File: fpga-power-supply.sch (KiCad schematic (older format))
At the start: 93 parts, among them U14 XC7A100T-FGG484

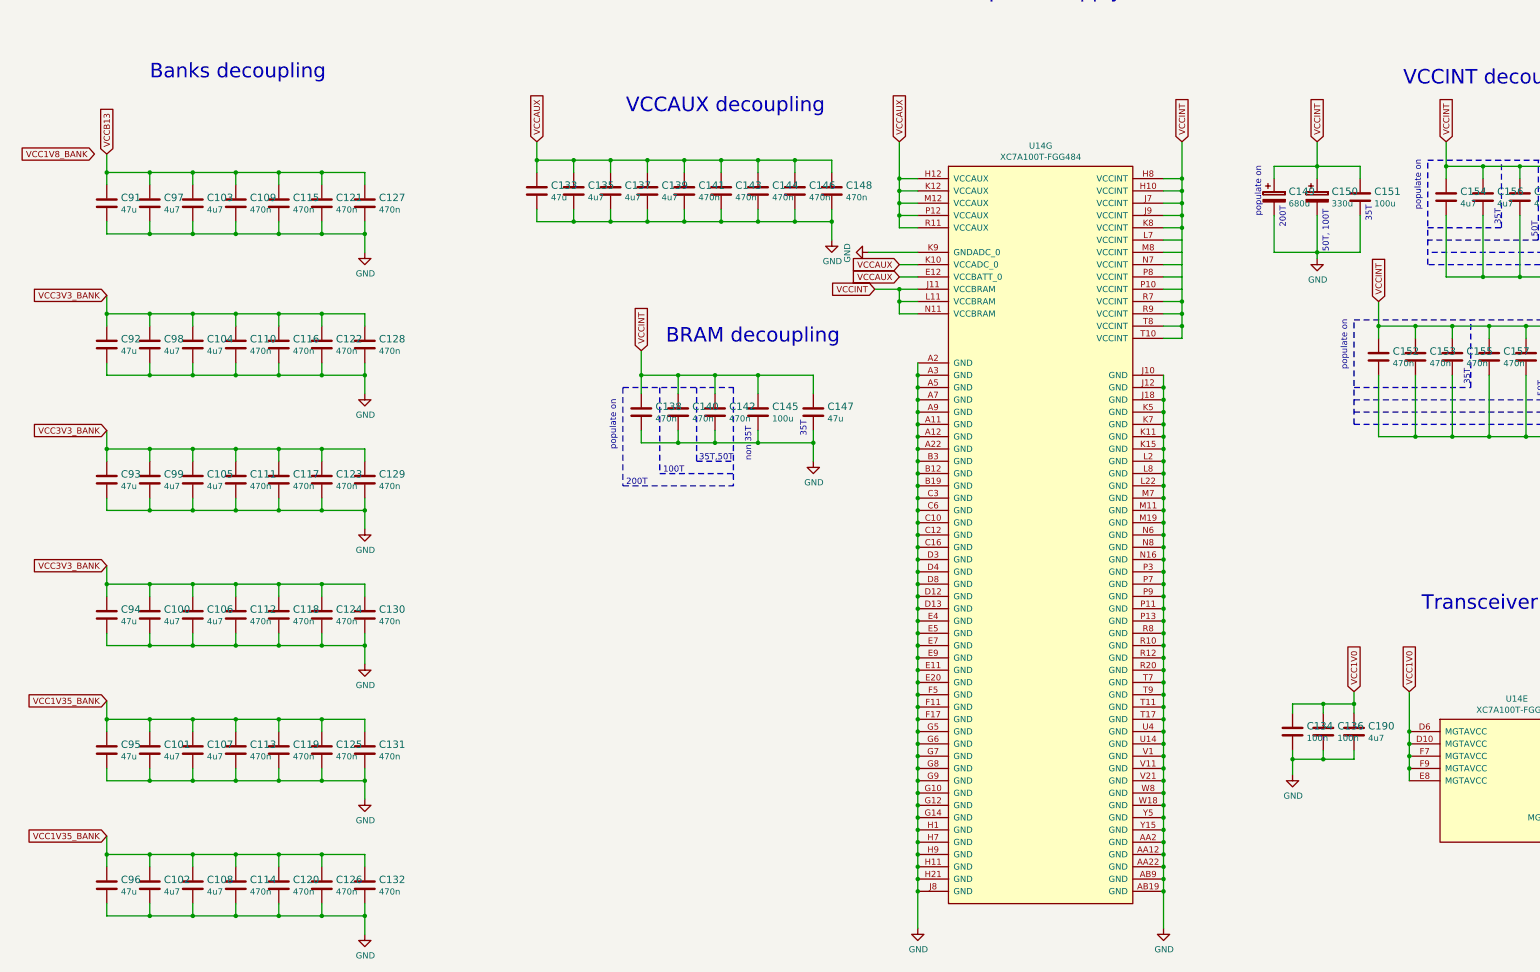
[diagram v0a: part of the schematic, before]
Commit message: Updated voltage supply labels, connected gpios left
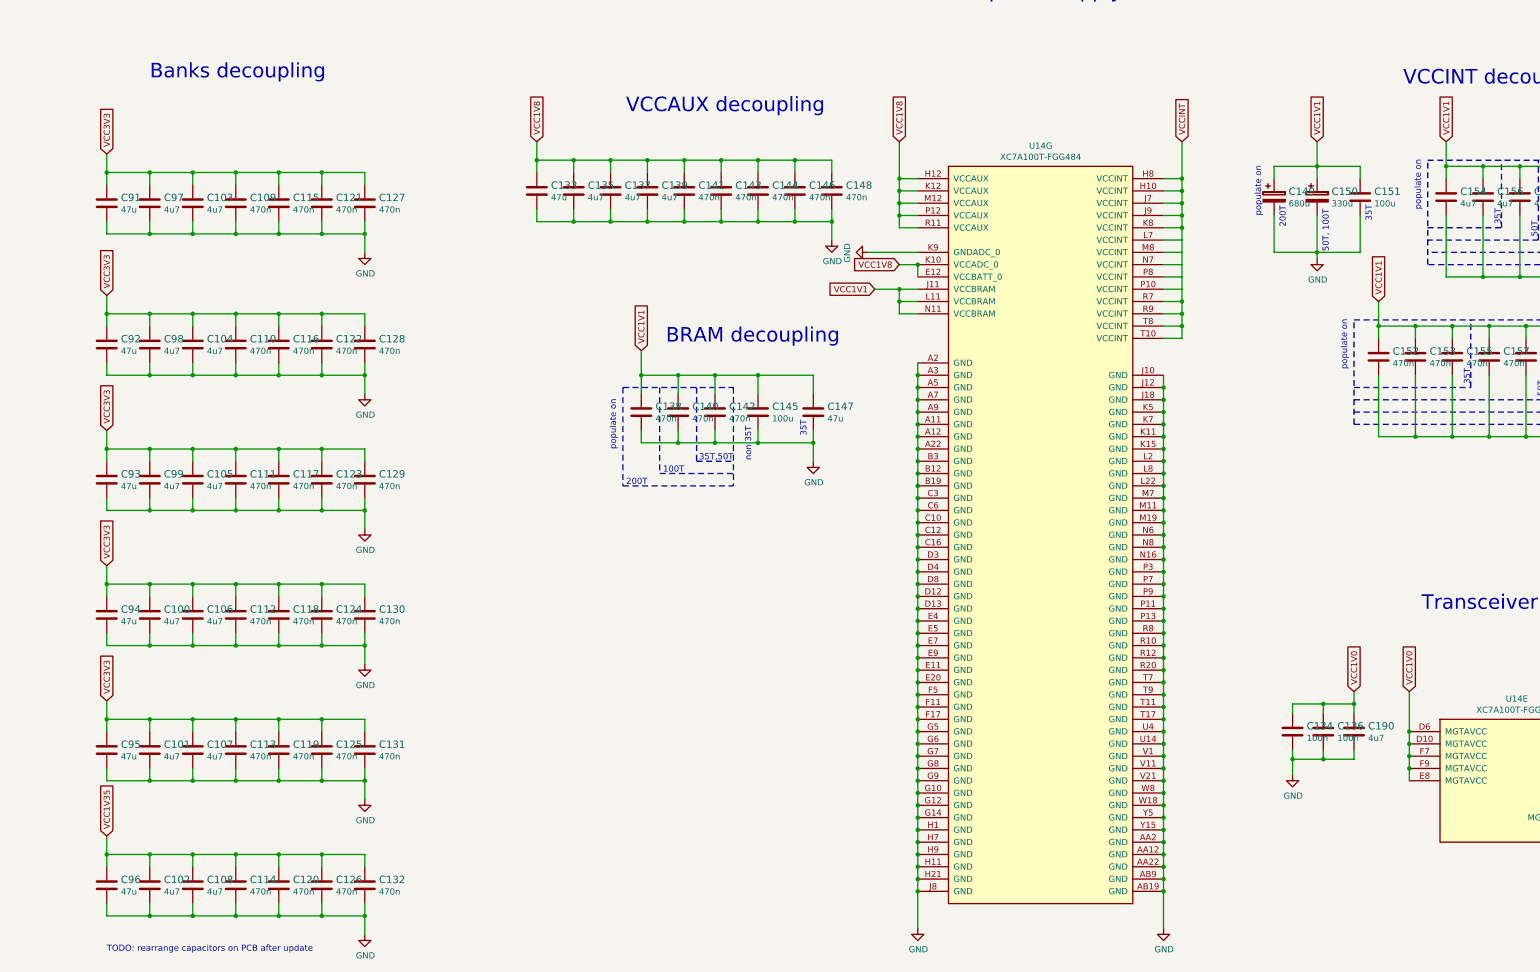
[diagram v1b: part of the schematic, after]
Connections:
- net VCCB13 is gone; now on net VCC3V3: C103.1, C109.1, C115.1, C121.1, C127.1, C91.1, C97.1
- net VCCINT: no longer C138.1, C140.1, C142.1, C145.1, C147.1, C149.1, C150.1, C151.1, C152.1, C153.1, C154.1, C155.1, C156.1, C157.1, C158.1, C159.1, C160.1, C161.1, C162.1, C163.1, C164.1, C165.1, C166.1, C167.1, C168.1, C169.1, C170.1, C171.1, C172.1, C173.1, C174.1, C175.1, C176.1, C177.1, U14.J11 (VCCBRAM), U14.L11 (VCCBRAM), U14.N11 (VCCBRAM)
- net VCC1V35_BANK renamed VCC1V35
- net VCC1V35: no longer C101.1, C107.1, C113.1, C119.1, C125.1, C131.1, C95.1
- net VCC3V3_BANK renamed VCC3V3
- net VCC3V3: now also C101.1, C107.1, C113.1, C119.1, C125.1, C131.1, C95.1
- net VCCAUX renamed VCC1V8
- new net VCC1V1: C138.1, C140.1, C142.1, C145.1, C147.1, C149.1, C150.1, C151.1, C152.1, C153.1, C154.1, C155.1, C156.1, C157.1, C158.1, C159.1, C160.1, C161.1, C162.1, C163.1, C164.1, C165.1, C166.1, C167.1, C168.1, C169.1, C170.1, C171.1, C172.1, C173.1, C174.1, C175.1, C176.1, C177.1, U14.J11 (VCCBRAM), U14.L11 (VCCBRAM), U14.N11 (VCCBRAM)
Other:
- note added: "TODO: rearrange capacitors on PCB after update"
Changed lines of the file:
@@
 	1150 2850 1150 2700
 Connection ~ 1150 2850
-Text GLabel 1150 2700 1    50   Input ~ 0
-VCCB13
 $Comp
 L artix-dc-scm:C_47u_1210 C?
@@
 	9900 4100 9900 4200
 Wire Wire Line
-	7750 3700 7600 3700
-Wire Wire Line
 	7750 3600 7600 3600
 $Comp
@@
 Text Notes 5375 2375 0    118  ~ 0
 VCCAUX decoupling
-Text GLabel 4650 2600 1    50   Input ~ 0
-VCCAUX
-Text GLabel 7600 2600 1    50   Input ~ 0
-VCCAUX
-Text GLabel 7600 3600 0    50   Input ~ 0
-VCCAUX
-Text GLabel 7600 3700 0    50   Input ~ 0
-VCCAUX
 Text GLabel 7400 3800 0    50   Input ~ 0
-VCCINT
-Text GLabel 5500 4300 1    50   Input ~ 0
-VCCINT
+VCC1V1
 Text GLabel 9900 2600 1    50   Input ~ 0
 VCCINT
-Text GLabel 11000 2600 1    50   Input ~ 0
-VCCINT
-Text GLabel 12050 2600 1    50   Input ~ 0
-VCCINT
-Text GLabel 11500 3900 1    50   Input ~ 0
-VCCINT
-Text GLabel 1050 2700 0    50   Input ~ 0
-VCC1V8_BANK
-Text GLabel 1150 4950 0    50   Input ~ 0
-VCC3V3_BANK
-Text GLabel 1150 6050 0    50   Input ~ 0
-VCC3V3_BANK
-Text GLabel 1150 7150 0    50   Input ~ 0
-VCC1V35_BANK
-Text GLabel 1150 8250 0    50   Input ~ 0
-VCC1V35_BANK
+Text GLabel 1150 7150 1    50   Input ~ 0
+VCC3V3
+Text GLabel 1150 8250 1    50   Input ~ 0
+VCC1V35
 $Comp
 L artix-dc-scm:C_4u7_0603 C?
@@
 Wire Wire Line
 	7350 3500 7750 3500
-Text GLabel 1150 3850 0    50   Input ~ 0
-VCC3V3_BANK
+Text GLabel 1150 3850 1    50   Input ~ 0
+VCC3V3
 $Comp
 L artix-dc-scm:XC7A100T-FGG484 U?
@@
 Text Notes 11850 6425 0    118  ~ 0
 Transceiver supply
+Text GLabel 7600 2600 1    50   Input ~ 0
+VCC1V8
+Text GLabel 7600 3600 0    50   Input ~ 0
+VCC1V8
+Wire Wire Line
+	7750 3600 7750 3700
+Connection ~ 7750 3600
+Text GLabel 4650 2600 1    50   Input ~ 0
+VCC1V8
+Text GLabel 1150 2700 1    50   Input ~ 0
+VCC3V3
+Text GLabel 1150 4950 1    50   Input ~ 0
+VCC3V3
+Text GLabel 1150 6050 1    50   Input ~ 0
+VCC3V3
+Text GLabel 5500 4300 1    50   Input ~ 0
+VCC1V1
+Text GLabel 11000 2600 1    50   Input ~ 0
+VCC1V1
+Text GLabel 12050 2600 1    50   Input ~ 0
+VCC1V1
+Text GLabel 11500 3900 1    50   Input ~ 0
+VCC1V1
+Text Notes 1150 9200 0    50   ~ 0
+TODO: rearrange capacitors on PCB after update
 $EndSCHEMATC

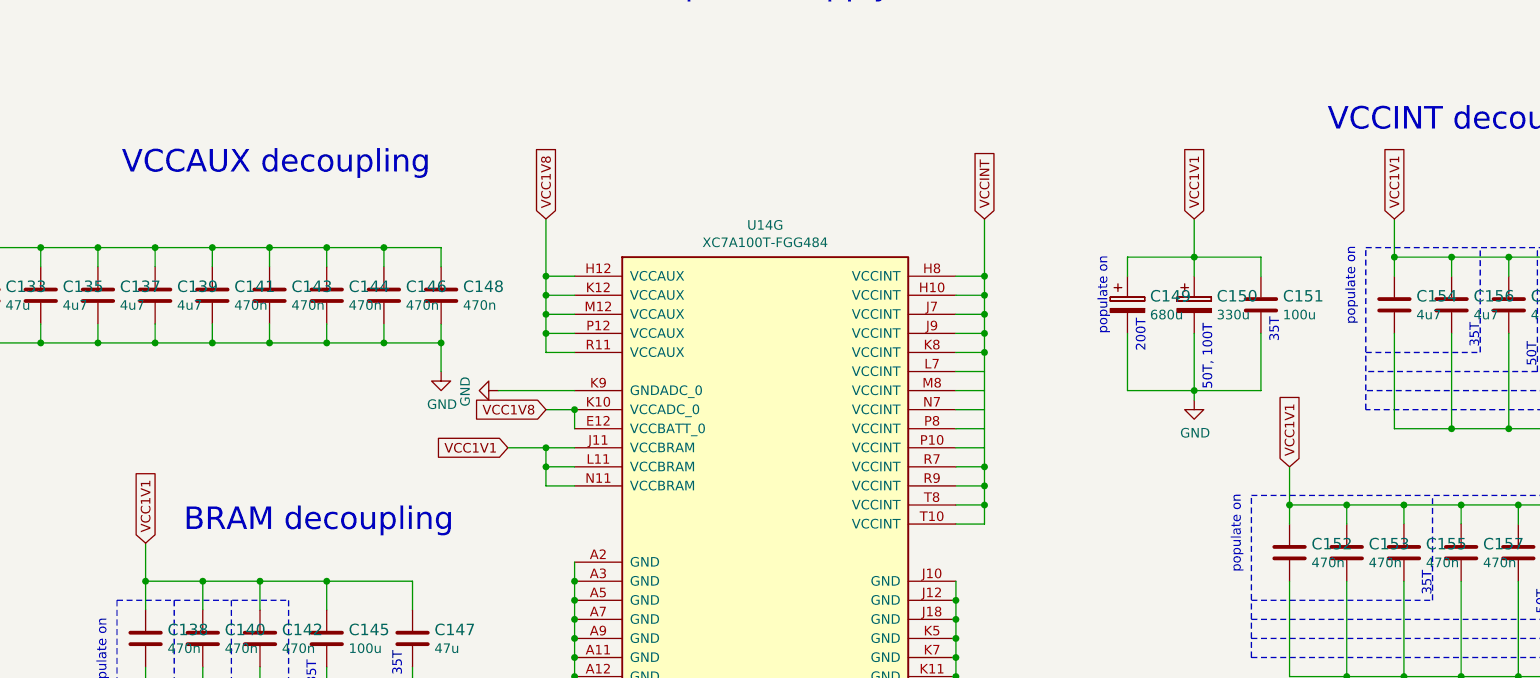
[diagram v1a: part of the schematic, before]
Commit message: Added power planes, set M.2 mounting hole position
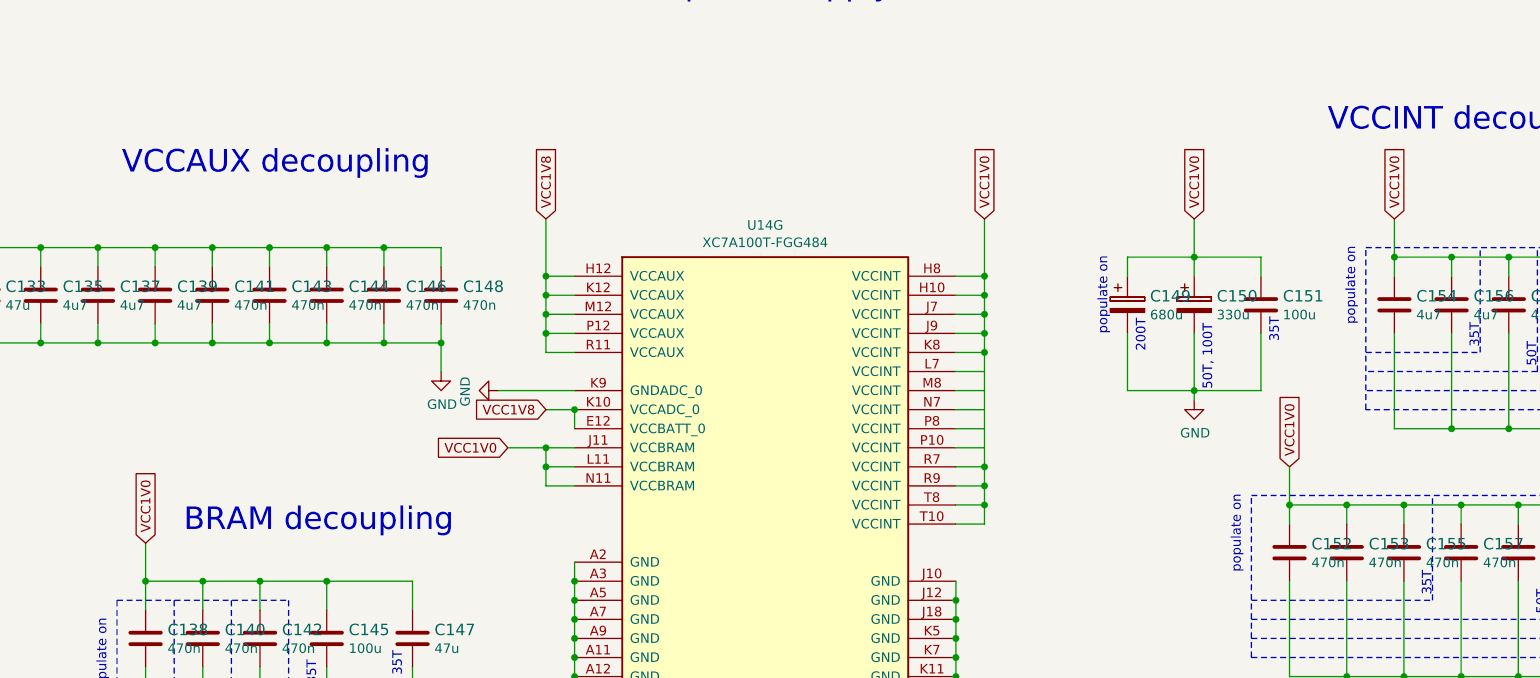
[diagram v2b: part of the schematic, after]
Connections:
- net VCC1V1 is gone; now on net VCC1V0: C138.1, C140.1, C142.1, C145.1, C147.1, C149.1, C150.1, C151.1, C152.1, C153.1, C154.1, C155.1, C156.1, C157.1, C158.1, C159.1, C160.1, C161.1, C162.1, C163.1, C164.1, C165.1, C166.1, C167.1, C168.1, C169.1, C170.1, C171.1, C172.1, C173.1, C174.1, C175.1, C176.1, C177.1, U14.J11 (VCCBRAM), U14.L11 (VCCBRAM), U14.N11 (VCCBRAM)
- net VCCINT is gone; now on net VCC1V0: U14.H10 (VCCINT), U14.H8 (VCCINT), U14.J7 (VCCINT), U14.J9 (VCCINT), U14.K8 (VCCINT), U14.R7 (VCCINT), U14.R9 (VCCINT), U14.T10 (VCCINT), U14.T8 (VCCINT)
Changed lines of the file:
@@
 VCCAUX decoupling
 Text GLabel 7400 3800 0    50   Input ~ 0
-VCC1V1
-Text GLabel 9900 2600 1    50   Input ~ 0
-VCCINT
+VCC1V0
 Text GLabel 1150 7150 1    50   Input ~ 0
 VCC3V3
@@
 VCC3V3
 Text GLabel 5500 4300 1    50   Input ~ 0
-VCC1V1
-Text GLabel 11000 2600 1    50   Input ~ 0
-VCC1V1
+VCC1V0
 Text GLabel 12050 2600 1    50   Input ~ 0
-VCC1V1
+VCC1V0
 Text GLabel 11500 3900 1    50   Input ~ 0
-VCC1V1
+VCC1V0
 Text Notes 1150 9200 0    50   ~ 0
 TODO: rearrange capacitors on PCB after update
+Text GLabel 9900 2600 1    50   Input ~ 0
+VCC1V0
+Text GLabel 11000 2600 1    50   Input ~ 0
+VCC1V0
 $EndSCHEMATC

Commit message: Update filtering capacitors
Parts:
- added C234, C235, C236, C237, C238, C239, C240: C_470n_0402, artix-dc-scm-footprints:0402-cap, symbol artix-dc-scm:C_470n_0402
- added C241: C_100n_0402, artix-dc-scm-footprints:0402-cap, symbol artix-dc-scm:C_100n_0402-artix-dc-scm
- added C242: C_470n_0402, antmicro-footprints:0201-res, symbol antmicroCapacitorsmisc:C_470n_0201
- C138, C142, C146, C152, C153, C157, C159, C161, C163, C165, C171, C175: footprint artix-dc-scm-footprints:0402-cap -> antmicro-footprints:0201-res; symbol artix-dc-scm:C_470n_0402 -> antmicroCapacitorsmisc:C_470n_0201; MPN C1005X5R1E474M050BB -> C0603X5R1A474M030BC
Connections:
- net GND: now also C234.2, C235.2, C236.2, C237.2, C238.2, C239.2, C240.2, C241.2, C242.2
- net VCC1V2: now also C241.1
- net VCC1V8: now also C242.1
- net VCC3V3: now also C234.1, C235.1, C236.1, C237.1, C238.1, C239.1, C240.1

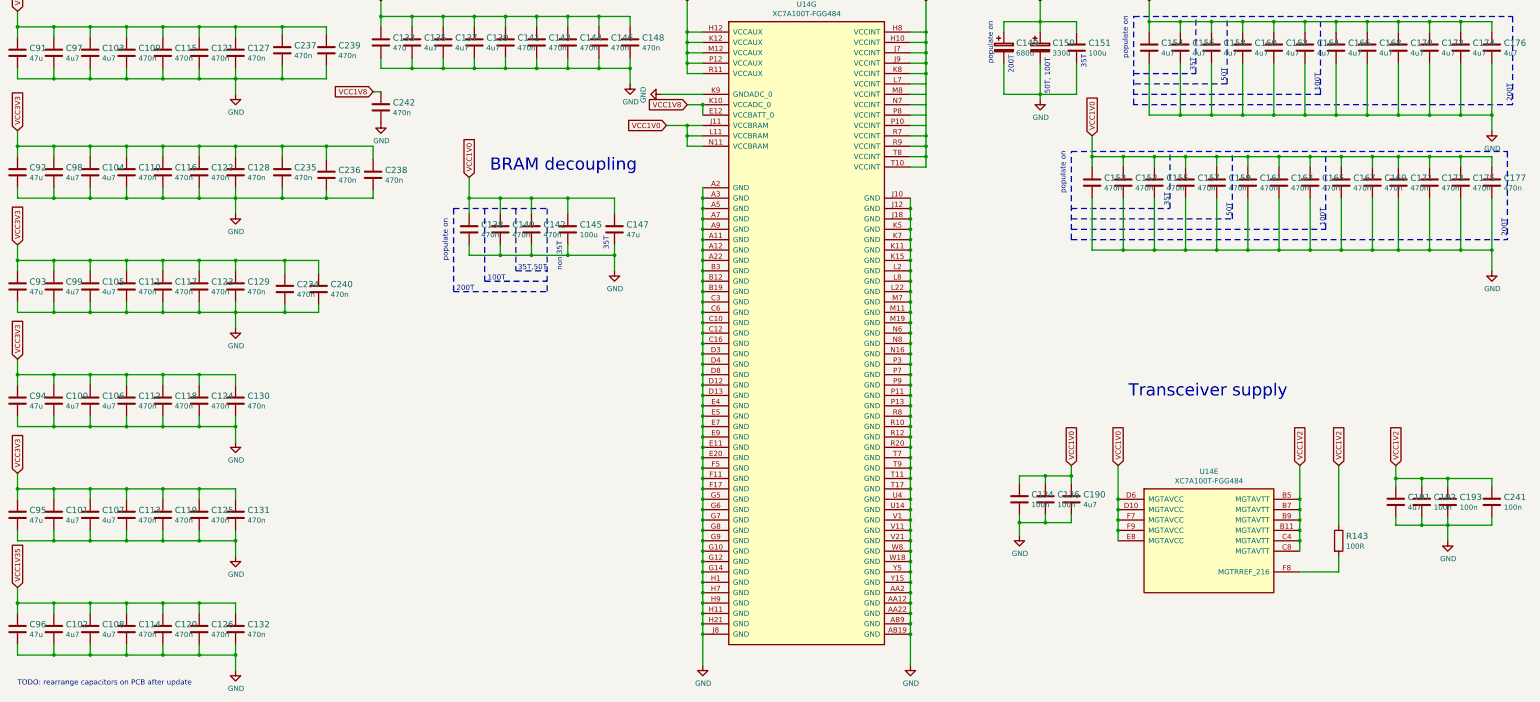
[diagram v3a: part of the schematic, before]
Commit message: Update DDR3 filtering
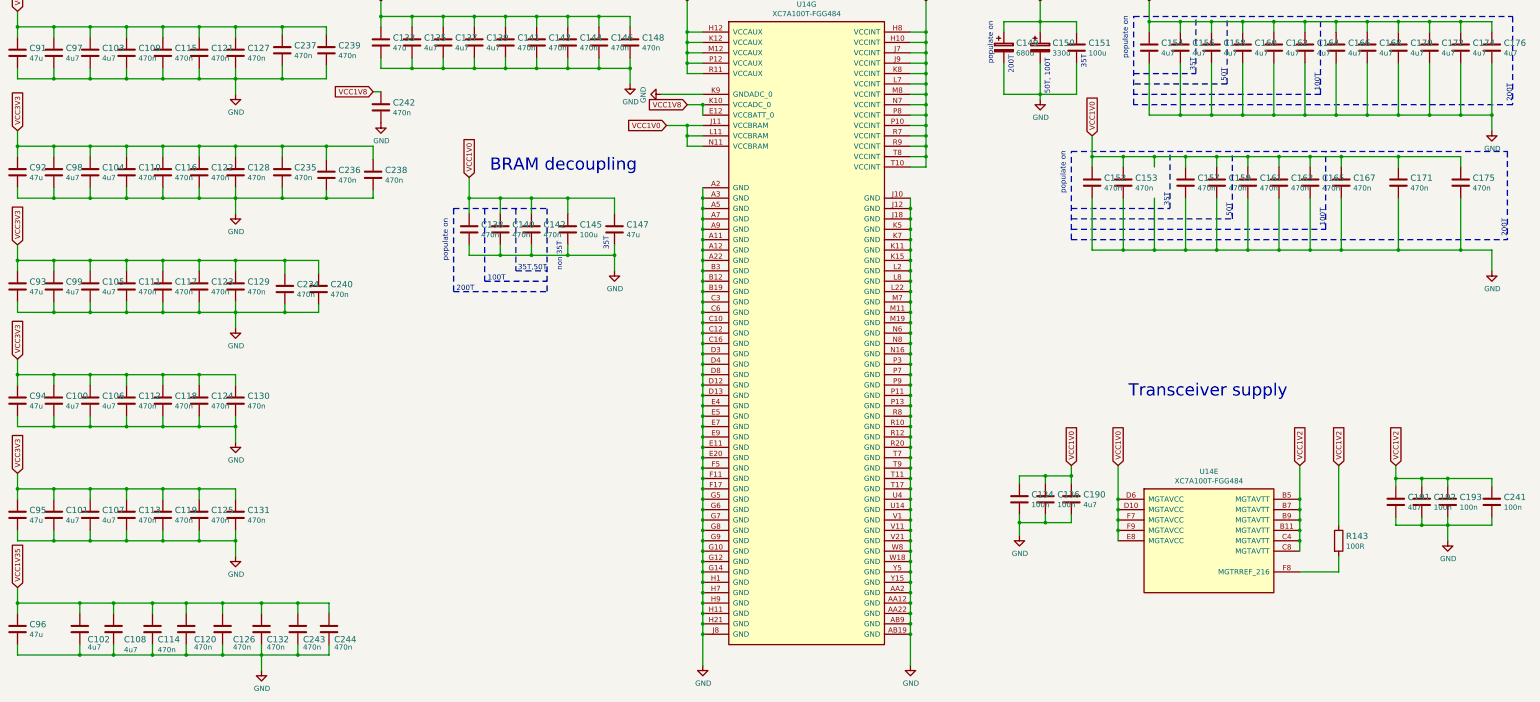
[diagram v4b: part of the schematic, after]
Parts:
- removed C155, C169, C173, C177: C_470n_0402, artix-dc-scm-footprints:0402-cap, symbol artix-dc-scm:C_470n_0402
- added C243, C244: C_470n_0402, artix-dc-scm-footprints:0402-cap, symbol artix-dc-scm:C_470n_0402
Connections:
- net GND: now also C243.2, C244.2
- net VCC1V0: now also U14.L7 (VCCINT), U14.M8 (VCCINT), U14.N7 (VCCINT), U14.P10 (VCCINT), U14.P8 (VCCINT)
- net VCC1V35: now also C243.1, C244.1
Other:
- note removed: "TODO: rearrange capacitors on PCB after update"
- moved on the sheet: C102, C108, C114, C120, C126, C132
